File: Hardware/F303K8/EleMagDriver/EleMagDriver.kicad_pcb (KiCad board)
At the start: 2 copper layers, 119.4 x 78.7 mm, 49 parts, among them IC1 TBD62083APG, IC2 TBD62083APG, IC3 TBD62083APG, J1 MIC_{IN}, J10 GuitarE, J11 GuitarF, J12 RelayA, J13 RelayB, J14 RelayC, J15 RelayD, J16 RelayE, J17 RelayF, J18 RelayG, J19 RelayH, J2 LED_{OUT}, J20 RelayI, J21 RelayJ, J22 Jack-DC, J23 FloppyA, J24 Floppy_Power, J25 FloppyB, J26 Floppy_Power, J3 DRV_{In}, J4 DRV_{OUT}, J5 StpMotor, J6 GuitarA, J7 GuitarB, J8 GuitarC, J9 GuitarD, U1 LM3914V, U2 NUCLEO-F303K8, U3 NJM7805FA

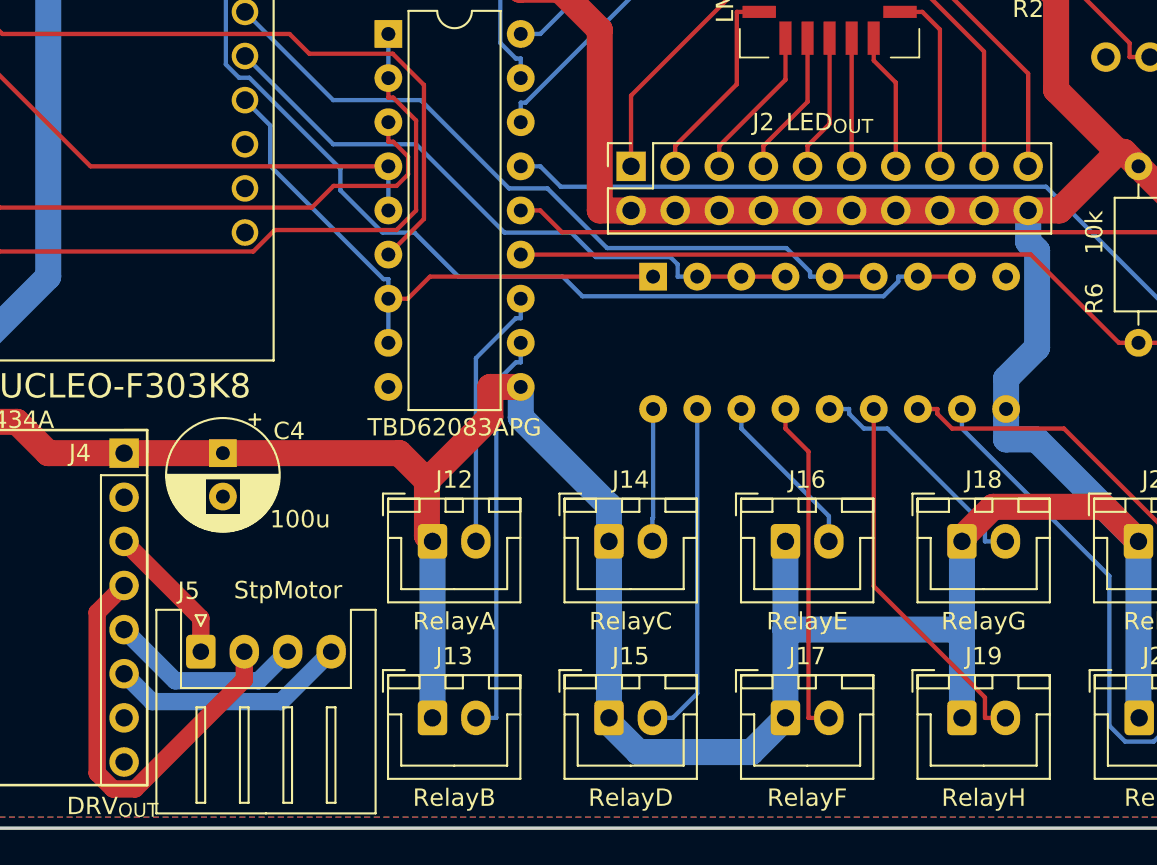
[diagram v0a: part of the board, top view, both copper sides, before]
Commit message: change stepping motor line
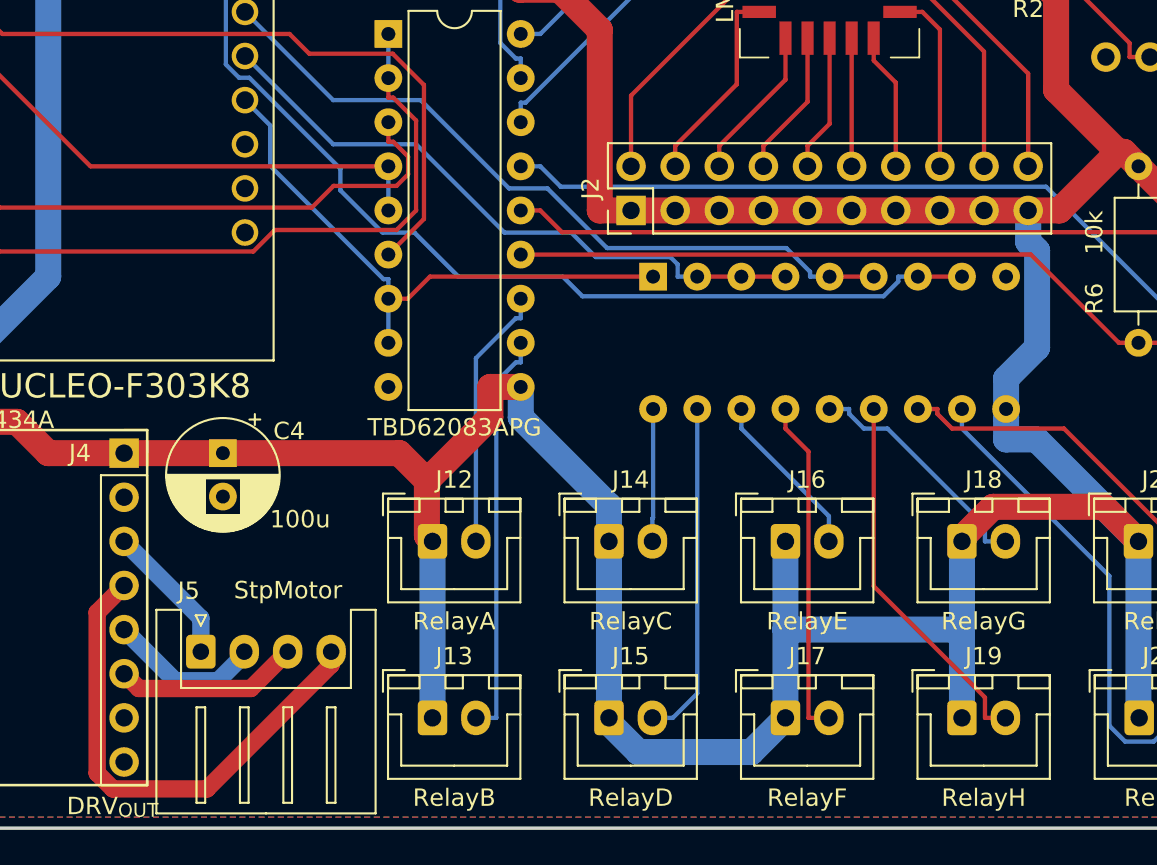
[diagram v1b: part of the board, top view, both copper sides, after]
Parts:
- J2: footprint Connector_PinSocket_2.54mm:PinSocket_2x10_P2.54mm_Vertical -> Connector_PinHeader_2.54mm:PinHeader_2x10_P2.54mm_Vertical
- moved J2 2.54 mm to (170.2, 92.7)
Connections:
- J2 pad 1: Net-(J2-Pin_1) -> +12V
- J2 pad 10: +12V -> Net-(J2-Pin_10)
- J2 pad 11: Net-(J2-Pin_11) -> +12V
- J2 pad 12: +12V -> Net-(J2-Pin_12)
- J2 pad 13: Net-(J2-Pin_13) -> +12V
- J2 pad 14: +12V -> Net-(J2-Pin_14)
- J2 pad 15: Net-(J2-Pin_15) -> +12V
- J2 pad 16: +12V -> Net-(J2-Pin_16)
- J2 pad 17: Net-(J2-Pin_17) -> +12V
- J2 pad 18: +12V -> Net-(J2-Pin_18)
- J2 pad 19: Net-(J2-Pin_19) -> +12V
- J2 pad 2: +12V -> Net-(J2-Pin_2)
- J2 pad 20: +12V -> Net-(J2-Pin_20)
- J2 pad 3: Net-(J2-Pin_3) -> +12V
- J2 pad 4: +12V -> Net-(J2-Pin_4)
- J2 pad 5: Net-(J2-Pin_5) -> +12V
- J2 pad 6: +12V -> Net-(J2-Pin_6)
- J2 pad 7: Net-(J2-Pin_7) -> +12V
- J2 pad 8: +12V -> Net-(J2-Pin_8)
- J2 pad 9: Net-(J2-Pin_9) -> +12V
- J4 pad 3: /Motor_OutB -> /Motor_OutA
- J4 pad 4: /Motor_OutBN -> /Motor_OutAN
- J4 pad 5: /Motor_OutAN -> /Motor_OutB
- J4 pad 6: /Motor_OutA -> /Motor_OutBN
- J5 pad 1: /Motor_OutB -> /Motor_OutA
- J5 pad 2: /Motor_OutBN -> /Motor_OutB
- J5 pad 3: /Motor_OutAN -> /Motor_OutBN
- J5 pad 4: /Motor_OutA -> /Motor_OutAN
- U1 pad 1: Net-(J2-Pin_19) -> Net-(J2-Pin_20)
- U1 pad 12: Net-(J2-Pin_1) -> Net-(J2-Pin_2)
- U1 pad 13: Net-(J2-Pin_3) -> Net-(J2-Pin_4)
- U1 pad 14: Net-(J2-Pin_5) -> Net-(J2-Pin_6)
- U1 pad 15: Net-(J2-Pin_7) -> Net-(J2-Pin_8)
- U1 pad 16: Net-(J2-Pin_9) -> Net-(J2-Pin_10)
- U1 pad 17: Net-(J2-Pin_11) -> Net-(J2-Pin_12)
- U1 pad 18: Net-(J2-Pin_13) -> Net-(J2-Pin_14)
- U1 pad 19: Net-(J2-Pin_15) -> Net-(J2-Pin_16)
- U1 pad 20: Net-(J2-Pin_17) -> Net-(J2-Pin_18)
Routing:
- net /Motor_OutAN: track 11.3 -> 29.0 mm
- net Net-(J2-Pin_20): track 0.00 -> 15.2 mm
- net Net-(J2-Pin_19): track 15.2 -> 0.00 mm
- net Net-(J2-Pin_2): track 0.00 -> 14.0 mm
- net Net-(J2-Pin_1): track 14.0 -> 0.00 mm
- net /Motor_OutBN: track 24.5 -> 10.7 mm
- net Net-(J2-Pin_18): track 0.00 -> 12.9 mm
- net Net-(J2-Pin_17): track 12.9 -> 0.00 mm
- net Net-(J2-Pin_4): track 0.00 -> 11.6 mm
- net Net-(J2-Pin_3): track 11.6 -> 0.00 mm
- net Net-(J2-Pin_16): track 0.00 -> 10.6 mm
- net Net-(J2-Pin_15): track 10.6 -> 0.00 mm
- net Net-(J2-Pin_6): track 0.00 -> 8.96 mm
- net Net-(J2-Pin_5): track 8.96 -> 0.00 mm
- net Net-(J2-Pin_8): track 0.00 -> 8.43 mm
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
